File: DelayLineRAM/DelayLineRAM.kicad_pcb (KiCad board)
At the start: 2 copper layers, 96 x 44.2 mm, 38 parts, among them J1 IO Connector Pins, Q1 NPN, U1 SR 1, U10 SR 10, U11 SR 11, U12 SR 12, U13 SR 13, U14 SR 14, U15 SR 15, U16 SR 16, U17 SR 17, U18 SR 18, U19 SR 19, U2 SR 2, U20 SR 20, U21 SR 21, U22 SR 22, U23 SR 23, U24 SR 24, U25 SR 25, U26 SR 26, U27 SR 27, U28 SR 28, U29 SR 29, U3 SR 3, U30 SR 30, U31 SR 31, U32 SR 32, U4 SR 4, U5 SR 5, U6 SR 6, U7 SR 7, U8 SR 8, U9 SR 9

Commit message: Finished the Address Counter PCB
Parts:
- added TP1: TestPoint, TestPoint:TestPoint_Pad_D1.5mm, B.Cu at (88.8, 40.2)
- added TP2: TestPoint, TestPoint:TestPoint_Pad_D1.5mm, B.Cu at (91.5, 40.2)
- added TP3: TestPoint, TestPoint:TestPoint_Pad_D1.5mm, B.Cu at (94.5, 40.2)
- added TP4: TestPoint, TestPoint:TestPoint_Pad_D1.5mm, B.Cu at (97.2, 40.2)
- added TP5: TestPoint, TestPoint:TestPoint_Pad_D1.5mm, B.Cu at (100.0, 40.2)
- added TP6: TestPoint, TestPoint:TestPoint_Pad_D1.5mm, B.Cu at (84.0, 56.2)
- added TP7: TestPoint, TestPoint:TestPoint_Pad_D1.5mm, B.Cu at (81.2, 54.2)
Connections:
- net Reset renamed Reset#
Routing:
- net DataOut: track 127.2 -> 146.8 mm, vias 1 -> 3
- net DataIn: track 59.0 -> 73.8 mm, vias 0 -> 2
- net Reset#: track 421.4 -> 431.1 mm
- net +5V: track 481.1 -> 488.9 mm
- net DoWrite: track 4.39 -> 9.25 mm
- net Clock: track 413.6 -> 416.9 mm, vias 32 -> 34

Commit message: changed ram connector to pin headers and created fab data for the delay line ram
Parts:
- J1: footprint Connector_Hirose:Hirose_DF13-07P-1.25DSA_1x07_P1.25mm_Vertical -> Connector_PinHeader_2.54mm:PinHeader_1x07_P2.54mm_Horizontal
- moved J1 18.0 mm to (81.5, 60.0), turned to 180 degrees
- moved TP6 16.1 mm to (80.5, 40.5)
- moved TP7 3.88 mm to (85.0, 53.2)
- moved R2 3.81 mm to (84.8, 61.8)
- moved Q1 3.00 mm to (82.0, 65.6)
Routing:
- net DoWrite: track 9.25 -> 17.5 mm
- net Reset#: track 431.1 -> 422.9 mm, vias 0 -> 1
- net DataOut: track 146.8 -> 141.6 mm, vias 3 -> 4
- net Net-(D2-A): track 25.1 -> 22.1 mm
- net Clock: track 416.9 -> 418.1 mm
- net +5V: track 488.9 -> 488.0 mm, vias 0 -> 1
- net DataIn: track 73.8 -> 73.6 mm, vias 2 -> 5
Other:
- board size 96 x 44.2 mm -> 97.8 x 44.2 mm
- board text added: "4/22/2026 Version 1.0"

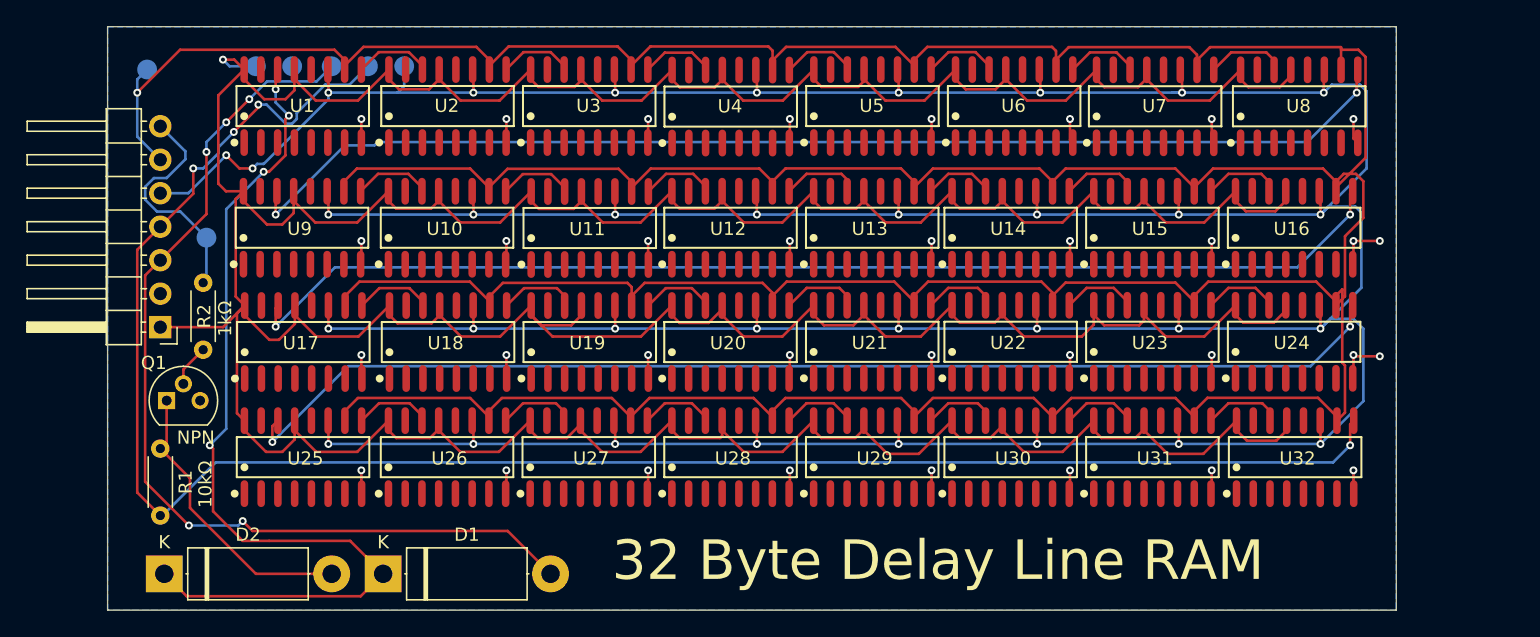
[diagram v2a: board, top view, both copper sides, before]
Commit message: Fixed the MUX for which data line to use when recirculating bits. Created the new FAB files for that too
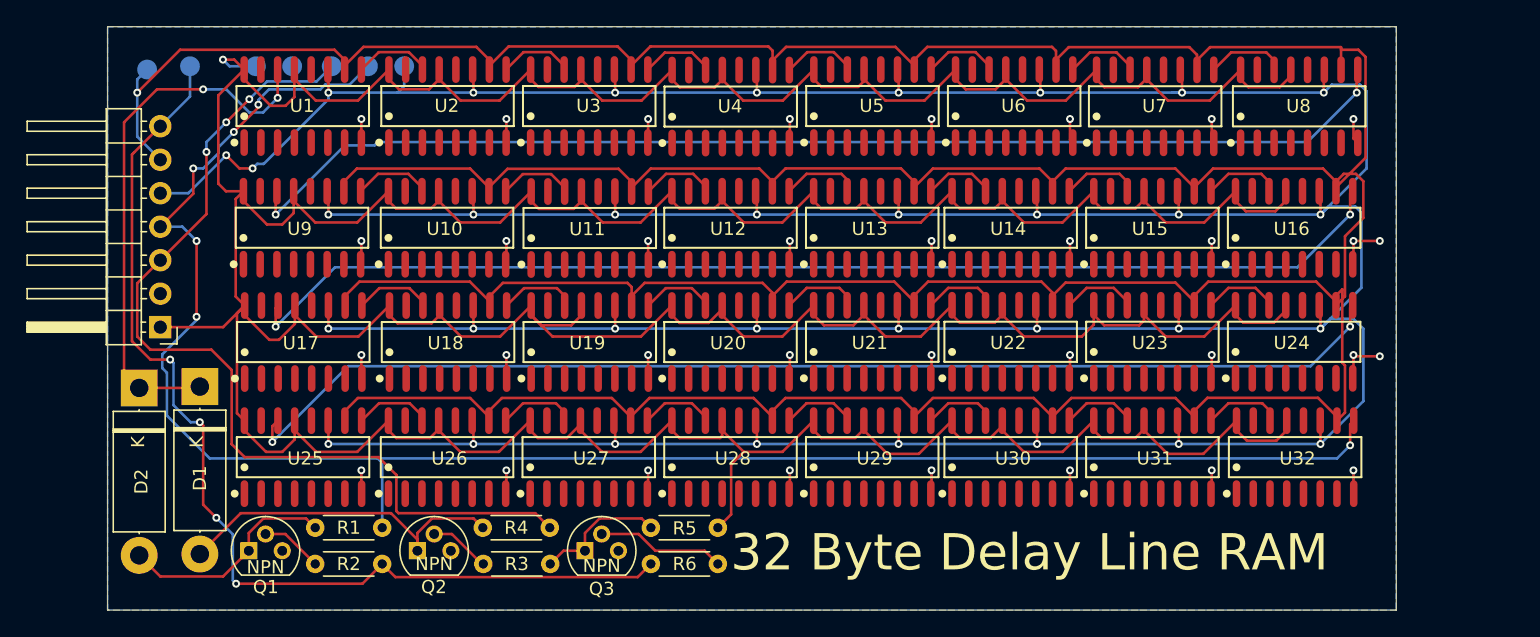
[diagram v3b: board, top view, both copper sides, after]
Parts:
- added Q2: NPN, Package_TO_SOT_THT:TO-92, F.Cu at (101.0, 77.0)
- added Q3: NPN, Package_TO_SOT_THT:TO-92, F.Cu at (113.7, 77.0)
- added R3: 1kOhm, Resistor_THT:R_Axial_DIN0204_L3.6mm_D1.6mm_P5.08mm_Horizontal, F.Cu at (106.0, 78.0)
- added R4: 1kOhm, Resistor_THT:R_Axial_DIN0204_L3.6mm_D1.6mm_P5.08mm_Horizontal, F.Cu at (106.0, 75.2)
- added R5: 1kOhm, Resistor_THT:R_Axial_DIN0204_L3.6mm_D1.6mm_P5.08mm_Horizontal, F.Cu at (118.7, 75.2)
- added R6: 1kOhm, Resistor_THT:R_Axial_DIN0204_L3.6mm_D1.6mm_P5.08mm_Horizontal, F.Cu at (118.7, 78.0)
- R1: value 10kOhm -> 1kOhm
- moved D1 19.9 mm to (84.5, 64.5), turned to -90 degrees
- moved R2 18.3 mm to (93.2, 78.0), turned to 0 degrees
- moved D2 14.2 mm to (79.9, 64.7), turned to -90 degrees
- moved R1 13.2 mm to (93.2, 75.2), turned to 0 degrees
- moved TP7 13.1 mm to (83.8, 40.2)
- moved Q1 13.0 mm to (88.2, 77.0)
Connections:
- net DoWrite renamed WriteEnable
- D1 pad 2: DataIn -> Net-(D1-A)
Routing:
- net WriteEnable: track 17.5 -> 78.5 mm, vias 0 -> 4
- net SR1_Write: track 69.7 -> 41.3 mm, vias 4 -> 2
- net Net-(D1-A): track 0.00 -> 26.5 mm
- net !WriteEnable: track 0.00 -> 10.1 mm
- net Net-(Q3-B): track 0.00 -> 9.75 mm
- net +5V: track 488.0 -> 495.3 mm
- net Net-(D2-A): track 22.1 -> 16.9 mm
- net Net-(Q2-B): track 0.00 -> 4.67 mm
- net DataIn: track 73.6 -> 71.0 mm, vias 5 -> 3
- net DataOut: track 141.6 -> 139.0 mm, vias 4 -> 6
- net Net-(Q1-B): track 3.21 -> 4.71 mm
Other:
- board text added: "Write Enable"
- board text removed: "10kΩ"
- board text removed: "1kΩ"
- board text removed: "Do Write"
- board text removed: "NPN"

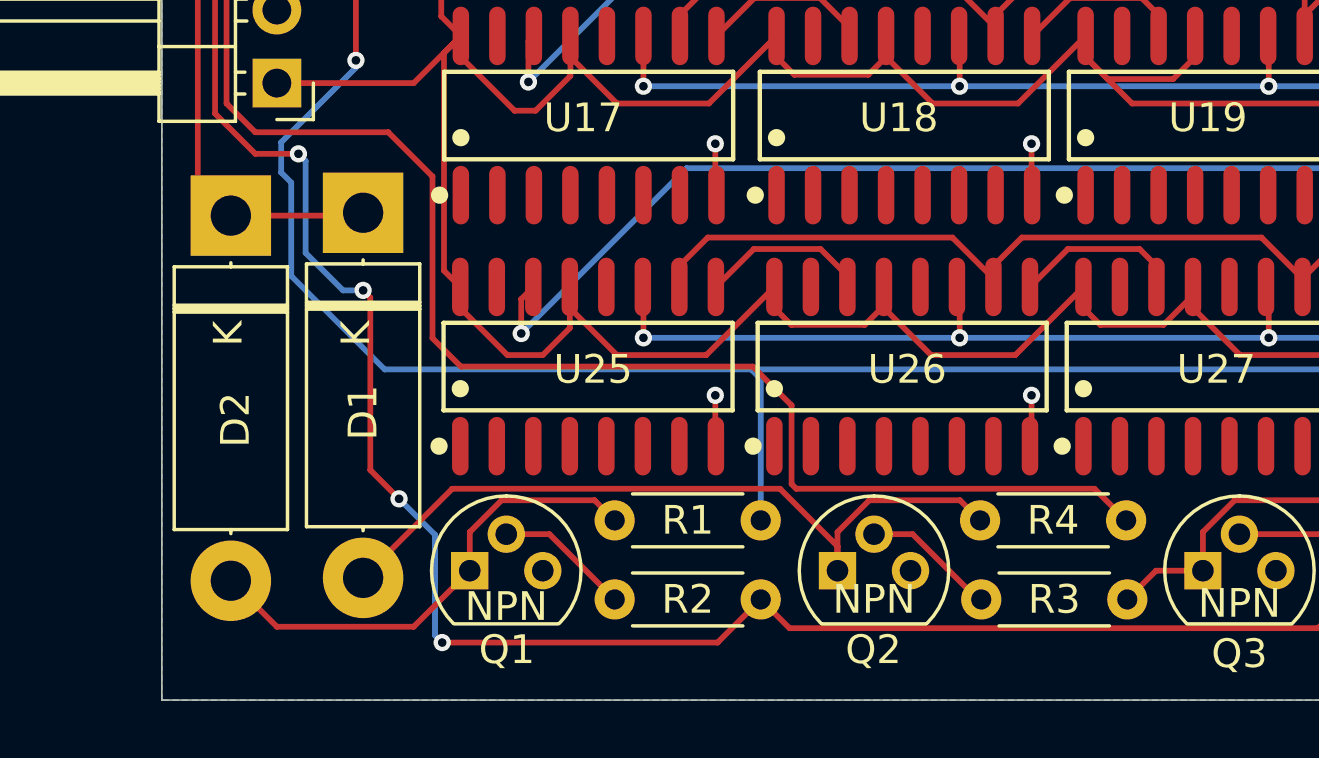
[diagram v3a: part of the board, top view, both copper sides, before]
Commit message: fixed the circuit in kicad for the schem and pcb
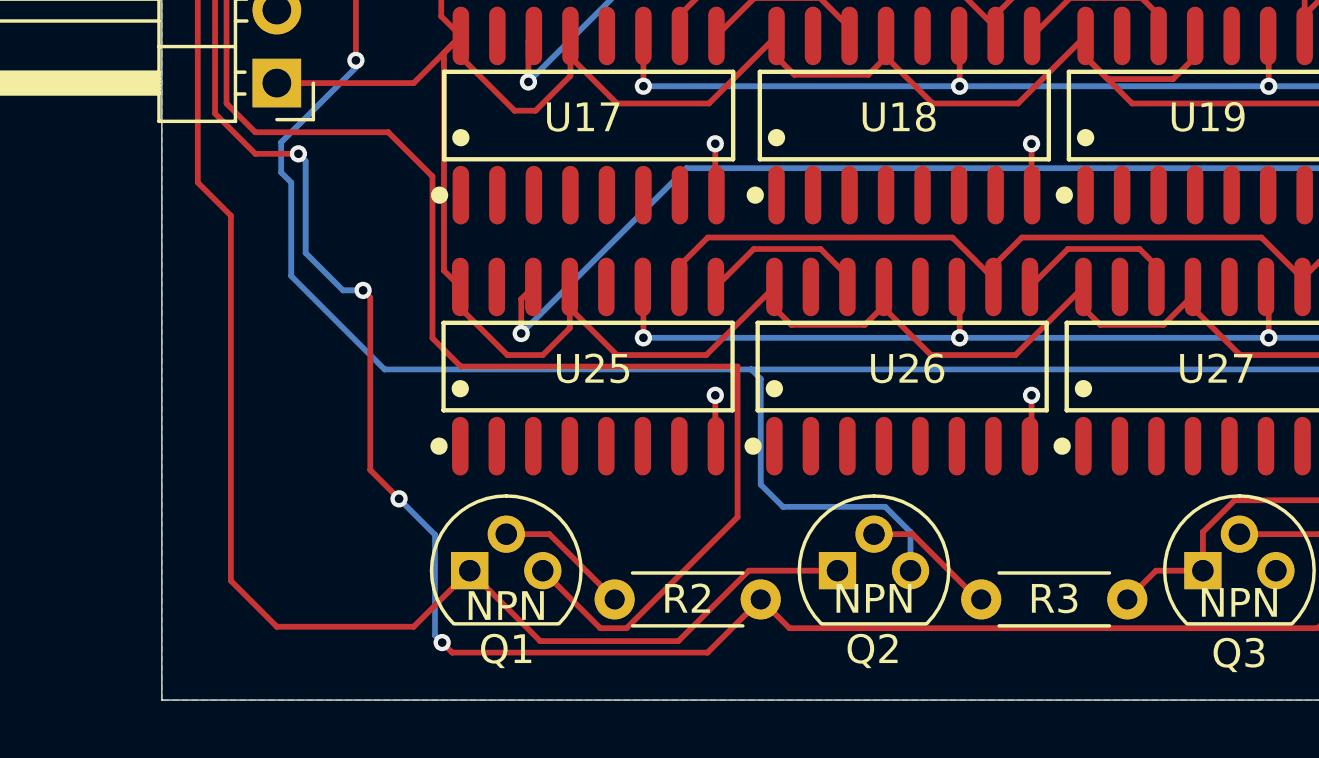
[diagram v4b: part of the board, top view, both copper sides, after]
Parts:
- removed D1, D2: D, Diode_THT:D_5W_P12.70mm_Horizontal
- removed R1, R4: 1kOhm, Resistor_THT:R_Axial_DIN0204_L3.6mm_D1.6mm_P5.08mm_Horizontal
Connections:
- Q1 pad 1: Net-(D2-A) -> SR1_Write
- Q1 pad 3: GND -> DataIn
- Q2 pad 1: Net-(D1-A) -> SR1_Write
- Q2 pad 3: GND -> DataOut
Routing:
- net SR1_Write: track 41.3 -> 73.9 mm
- net Net-(D1-A): track 26.5 -> 0.00 mm
- net Net-(D2-A): track 16.9 -> 0.00 mm
- net DataOut: track 139.0 -> 145.0 mm
- net DataIn: track 71.0 -> 68.1 mm
